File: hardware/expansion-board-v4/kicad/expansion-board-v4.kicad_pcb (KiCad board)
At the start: 6 copper layers, 100 x 62 mm, 174 parts, among them J1 PinHeader_2x20_P2.54mm_Vertic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, J2 U.FL_Hirose_U.FL-R-SMT-1_Vert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, J4 USB_C_Receptacle_HRO_TYPE-C-3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, J5 U.FL_Hirose_U.FL-R-SMT-1_Vert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, J6 U.FL_Hirose_U.FL-R-SMT-1_Vert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, J7 U.FL_Hirose_U.FL-R-SMT-1_Vert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, J8 U.FL_Hirose_U.FL-R-SMT-1_Vert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, J9 MX1.25WT-2P, Q2 SOT-23, Q3 SOT-23, Q4 SOT-23, Q5 SOT-23, SW2 SolderJumper-2_P1.3mm_Open_Pa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, U1 SOT-23-5, U10 QFN-48-1EP_7x7mm_P0.5mm_EP5.1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, U11 DFN-8-1EP_2x2mm_P0.5mm_EP0.86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, U12 SOT-363_SC-70-6, U13 AD8319_LFCSP-8-EP, U14 MSOP-8_3x3mm_P0.65mm, U15 SOT-23-6, U16 SOT-363_SC-70-6, U17 SOT-363_SC-70-6, U18 SOIC-10_3.9x4.9mm_P1mm, U19 QFN-24-1EP_4x4mm_P0.5mm_EP2.6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, U2 SOT-23-5, U20 TSOT-23-6, U3 SOT-23-5, U4 BNO085_LGA-28, U5 BMP388_LGA-10, U6 LGA-16_3x3mm_P0.5mm, U7 ATGM336H_LCC-18, U8 QFN-56-1EP_7x7mm_P0.4mm_EP3.2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, U9 SOIC-8_5.3x5.3mm_P1.27mm, Y1 Crystal_SMD_3225-4Pin_3.2x2.5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, Y2 Crystal_SMD_3225-4Pin_3.2x2.5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, Y3 Crystal_SMD_3215-2Pin_3.2x1.5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

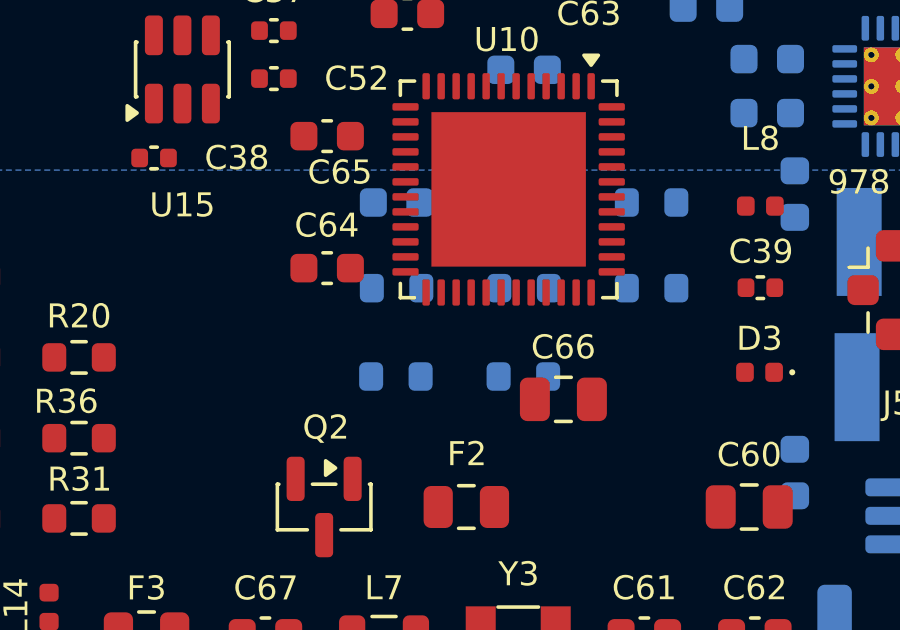
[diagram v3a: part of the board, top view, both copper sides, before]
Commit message: fix(hw): 103AT-2 是插件不是贴片，封装/焊盘/位置全部修正
## 主 bug：RT1 用错封装

103AT-2（SEMITEC 日本石塚）是**轴向引线玻璃封装的插件**，我之前直接套了
R_0603_1608Metric——焊盘、3D、装配全错，根因是没查 datasheet。

改为自建 NTC_103AT-2_Leaded_P2.54mm：两个 ⌀0.7 通孔、间距 2.54mm，
courtyard 只覆盖焊盘不含本体——因为 NTC 玻璃头不留在板面，靠引线延伸
平贴到电池表面。

位置从 (136.93,87.93) 改到 **(125.5,89.5)**，两个判据：
  · CHG_NTC 到分压电阻 R39/R40 只有 4.06mm。这是高阻模拟节点，
    原位置离分压网络 30mm，长走线会耦合开关噪声
  · 焊盘落在电池投影区内，玻璃头平贴板面与电池之间（电池仓净高 11.0
    − 电池 9.5 = 1.5mm 余量，刚好容下 ⌀1.5mm 玻璃头），热耦合最好

选点时扫描了两面 courtyard（通孔件会穿透）、螺丝孔让位圈、天线禁铺区。

## 连带修复：.kicad_mod 不能写 ';;' 注释

上一轮给 MX1.25WT-2P 封装加 3D 说明时用了 ';;'，那是 Lisp 语法，
KiCad 的 S-expression 解析器不认——**整个封装文件直接加载失败**，
而且不报错，只是 FootprintLoad 返回 None。逐个测试库中封装才发现
MX1.25WT-2P 和新建的 NTC 两个都是坏的。注释一律移进 (descr ...)。

## Python 环境：按 CLAUDE.md 用 ServBay

之前 gen_bom_smt.py 报缺 openpyxl，是因为我用了 KiCad 内置的 Python
（那个只该用于需要 pcbnew 的脚本）。ServBay 的 python3 3.13.12 本来就有
openpyxl 3.1.5。现在分工明确：
  · 需要 pcbnew 的（gen_assembly/gen_checklist）→ KiCad Python
  · 纯数据处理的（gen_bom/gen_bom_smt）→ ServBay Python

BOM_采购清单.xlsx（55 项）与 BOM_嘉立创SMT.xlsx（79 料号/162 贴片位）已补出。

## 新增待决项 D3：电源区电容建议 0603 → 0805

不是为了散热（电阻功率算过，R43 最大也才 32.5mW，0603 有 3 倍余量），
而是 DC bias 衰减和耐压可得性：**C72 要 6.8µF/25V，0603 根本买不到**
（0603 在 25V 档容值上限约 1~2.2µF），而它接 9V 侧耐压不能降。
换封装会动 B 面布局，等确认。

验收：原理图↔PCB 封装零不一致，DRC error 0 条，覆铜已重填。
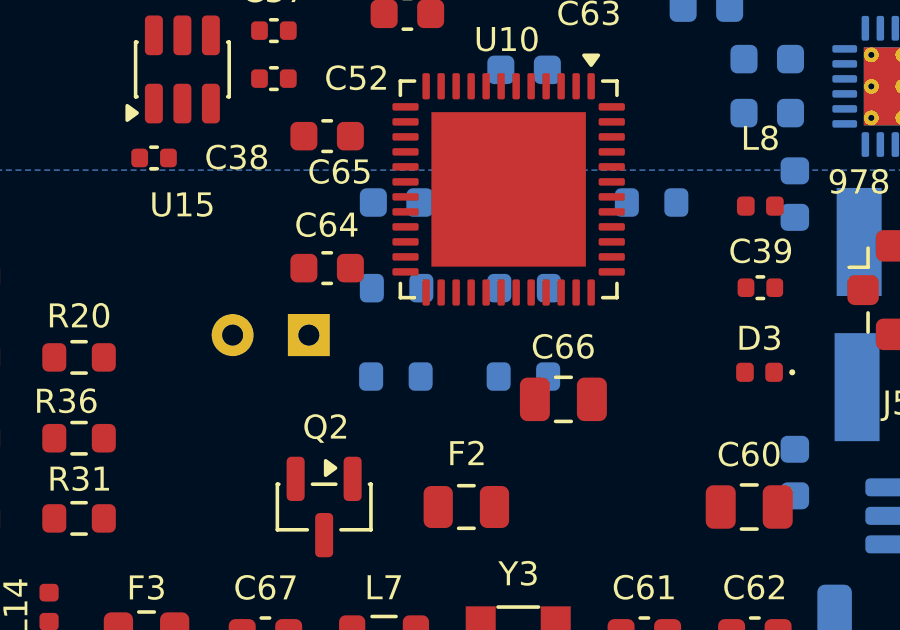
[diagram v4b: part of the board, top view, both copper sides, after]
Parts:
- RT1: value R_0603_1608Metric -> 103AT-2 10k NTC; footprint R_0603_1608Metric -> NTC_103AT-2_Leaded_P2.54mm
- moved RT1 11.5 mm to (125.5, 89.5), turned to 180 degrees
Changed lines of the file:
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@@
 		)
 	)
-	(footprint "R_0603_1608Metric"
+	(footprint "NTC_103AT-2_Leaded_P2.54mm"
 		(layer "B.Cu")
-		(at 136.925 87.9348)
-		(descr "Resistor SMD 0603 (1608 Metric), square (rectangular) end terminal, IPC-7351 nominal, (Body size source: IPC-SM-782 page 72, https://www.pcb-3d.com/wordpress/wp-content/uploads/ipc-sm-782a_amendment_1_and_2.pdf)")
-		(tags "resistor")
+		(at 125.5 89.5 180)
+		(descr "103AT-2 / 103AP-2 热敏电阻（SEMITEC 日本石塚）的板上焊盘。这是**轴向引线玻璃封装的插件**，不是贴片——2026-08-23 之前误用了 R_0603_1608Metric，焊盘和 3D 全错。玻璃头 ⌀约1.5mm、引线 ⌀0.2mm 长约 25~30mm。本封装只画两个通孔焊盘：NTC 本体**不留在板面**，靠引线延伸贴到电池表面并用胶带固定，因此 courtyard 只覆盖焊盘、不含器件本体。")
+		(tags "NTC thermistor 103AT-2 THT leaded battery temperature")
 		(property "Reference" "RT1"
-			(at 0.005 -1.4428 0)
+			(at 1.27 2.2 0)
 			(layer "B.SilkS")
 			(effects
@@
 			)
 		)
-		(property "Value" "R_0603_1608Metric"
-			(at 0 -1.43 180)
+		(property "Value" "103AT-2 10k NTC"
+			(at 1.27 -4.4 0)
 			(layer "B.Fab")
 			(effects
 				(font
-					(size 1 1)
+					(size 0.8 0.8)
 					(thickness 0.15)
 				)
@@
 		)
 		(property "Datasheet" ""
-			(at 0 0 180)
+			(at 0 0 0)
 			(layer "B.Fab")
 			(hide yes)
@@
 		)
 		(property "Description" ""
-			(at 0 0 180)
+			(at 0 0 0)
 			(layer "B.Fab")
 			(hide yes)
@@
 			)
 		)
-		(property "KiLib_Generator" "SMD_2terminal_chip_molded"
-			(at 0 0 180)
-			(layer "B.SilkS")
-			(hide yes)
-			(effects
-				(font
-					(size 1 1)
-					(thickness 0.15)
-				)
-				(justify mirror)
-			)
-		)
-		(attr smd)
+		(attr through_hole)
 		(duplicate_pad_numbers_are_jumpers no)
 		(fp_line
-			(start -0.237258 -0.5225)
-			(end 0.237258 -0.5225)
+			(start 3.64 1.1)
+			(end 3.64 -1.1)
 			(stroke
 				(width 0.12)
@@
 		)
 		(fp_line
-			(start -0.237258 0.5225)
-			(end 0.237258 0.5225)
+			(start -1.1 1.1)
+			(end 3.64 1.1)
 			(stroke
 				(width 0.12)
@@
 			(layer "B.SilkS")
 		)
-		(fp_rect
-			(start -1.48 0.73)
-			(end 1.48 -0.73)
+		(fp_line
+			(start -1.1 1.1)
+			(end -1.1 -1.1)
+			(stroke
+				(width 0.12)
+				(type solid)
+			)
+			(layer "B.SilkS")
+		)
+		(fp_line
+			(start -1.1 -1.1)
+			(end 3.64 -1.1)
+			(stroke
+				(width 0.12)
+				(type solid)
+			)
+			(layer "B.SilkS")
+		)
+		(fp_line
+			(start 3.89 1.35)
+			(end 3.89 -1.35)
 			(stroke
 				(width 0.05)
 				(type solid)
 			)
-			(fill no)
 			(layer "B.CrtYd")
 		)
-		(fp_rect
-			(start -0.8 0.4125)
-			(end 0.8 -0.4125)
+		(fp_line
+			(start 3.89 -1.35)
+			(end -1.35 -1.35)
+			(stroke
+				(width 0.05)
+				(type solid)
+			)
+			(layer "B.CrtYd")
+		)
+		(fp_line
+			(start -1.35 1.35)
+			(end 3.89 1.35)
+			(stroke
+				(width 0.05)
+				(type solid)
+			)
+			(layer "B.CrtYd")
+		)
+		(fp_line
+			(start -1.35 -1.35)
+			(end -1.35 1.35)
+			(stroke
+				(width 0.05)
+				(type solid)
+			)
+			(layer "B.CrtYd")
+		)
+		(fp_line
+			(start 3.64 1.1)
+			(end 3.64 -1.1)
 			(stroke
 				(width 0.1)
 				(type solid)
 			)
-			(fill no)
 			(layer "B.Fab")
 		)
-		(fp_text user "${REFERENCE}"
-			(at 0 0 180)
+		(fp_line
+			(start 3.64 -1.1)
+			(end -1.1 -1.1)
+			(stroke
+				(width 0.1)
+				(type solid)
+			)
 			(layer "B.Fab")
+		)
+		(fp_line
+			(start -1.1 1.1)
+			(end 3.64 1.1)
+			(stroke
+				(width 0.1)
+				(type solid)
+			)
+			(layer "B.Fab")
+		)
+		(fp_line
+			(start -1.1 -1.1)
+			(end -1.1 1.1)
+			(stroke
+				(width 0.1)
+				(type solid)
+			)
+			(layer "B.Fab")
+		)
+		(fp_text user "NTC->BAT"
+			(at 1.27 -2.3 0)
+			(layer "B.SilkS")
 			(effects
 				(font
-					(size 0.4 0.4)
-					(thickness 0.06)
+					(size 0.6 0.6)
+					(thickness 0.1)
 				)
 				(justify mirror)
 			)
 		)
-		(pad "1" smd roundrect
-			(at -0.825 0)
-			(size 0.8 0.95)
-			(layers "B.Cu" "B.Mask" "B.Paste")
-			(roundrect_rratio 0.25)
+		(pad "1" thru_hole rect
+			(at 0 0 180)
+			(size 1.4 1.4)
+			(drill 0.7)
+			(layers "*.Cu" "*.Mask")
+			(remove_unused_layers no)
 			(net "CHG_NTC")
 		)
-		(pad "2" smd roundrect
-			(at 0.825 0)
-			(size 0.8 0.95)
-			(layers "B.Cu" "B.Mask" "B.Paste")
-			(roundrect_rratio 0.25)
+		(pad "2" thru_hole circle
+			(at 2.54 0 180)
+			(size 1.4 1.4)
+			(drill 0.7)
+			(layers "*.Cu" "*.Mask")
+			(remove_unused_layers no)
 			(net "GND")
 		)
 		(embedded_fonts no)
-		(model "${KICAD10_3DMODEL_DIR}/Resistor_SMD.3dshapes/R_0603_1608Metric.step"
-			(offset
-				(xyz 0 0 0)
-			)
-			(scale
-				(xyz 1 1 1)
-			)
-			(rotate
-				(xyz 0 0 0)
-			)
-		)
 	)
 	(footprint "R_0603_1608Metric"

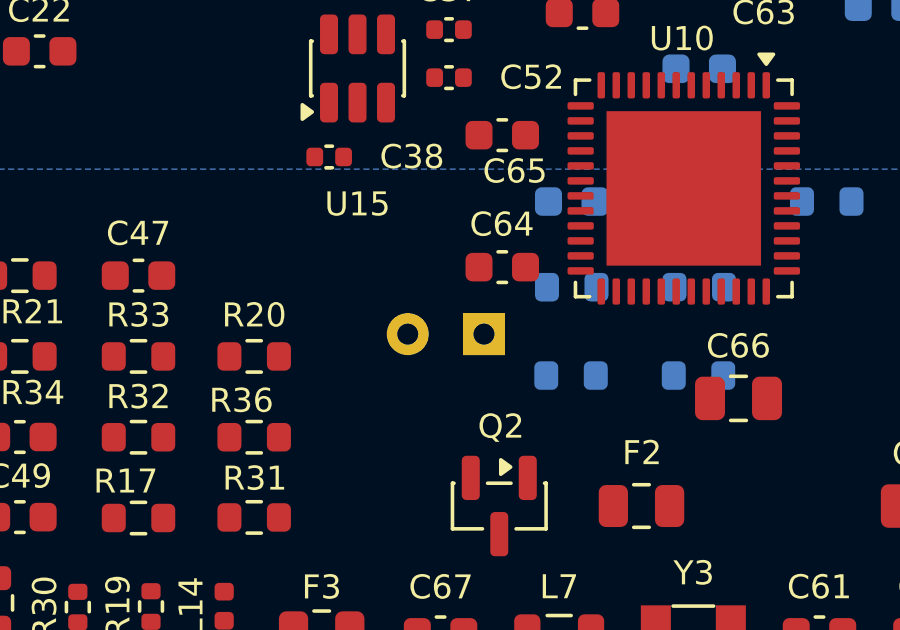
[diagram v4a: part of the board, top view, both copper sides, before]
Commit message: fix(hw): NTC 改用贴片 NCP18XH103F03RB —— 电池是 3M 胶贴死的，插件放不下
## 为什么又改一次

上一轮把 RT1 从 R0603 改成插件封装，理由是「103AT-2 是轴向引线玻璃件」。
那步是对的，但方案错了：**电池用 3M 胶直接贴在 B 面**（防晃动脱落，同时给
背壳散热孔留空间），板面与电池之间**没有间隙**，玻璃头无处安放。
我上一版假设有 1.5mm 余量（11.0 电池仓 − 9.5 电池），那是"电池悬空"的算法，
与实际装配方式不符。

回到贴片，但换成真正的贴片 NTC 型号，不是拿普通电阻封装凑数：
NCP18XH103F03RB（Murata 0603 10k 1%）/ TDK NTCG163JF103FT1 / 国产 0603 10K 1%。

## NTC 本身不能删

SY6970 的 TS 是锂电池充电安全强制项：<0°C 充电析锂（枝晶刺穿隔膜、内短路），
>60°C 加速老化乃至热失控。不接就得用固定电阻假装永远 25°C，等于关掉保护。

座舱 80°C 的担心已查证：TS 保护**只作用于充电路径**。高温时停充，但
PMID→SYS 直供与 BAT→SYS 放电都不受限，设备照常运行，降温自动恢复。
去掉 NTC 才会在 80°C 继续充电，那才是不可预测的后果。

## B 值差异不需要改硬件

103AT-2 是 B25/85=3435K；Murata NCP18XH103 常标 B25/50=3380K，
但同一颗料在 B25/85 口径下是 3428K——差 0.2%，保护阈值偏移 <1°C，
分压电阻 R39/R40 保持不变。要抠精度改 MCU 侧查表/Steinhart-Hart 的 B 参数。

## 位置 (125.25, 88.00)

三个约束一起解出来的：在电池投影区内直接贴电池 / 距板上开关电源 ≥19mm
（否则测的是板温不是电池温）/ CHG_NTC 到分压电阻 R39/R40 仅 4.00mm
（高阻模拟节点，走线长了耦合开关噪声）。

已删除废弃的 NTC_103AT-2_Leaded_P2.54mm 封装，免得下次误用。

验收：DRC error 0 条，原理图↔PCB 一致，全套 BOM/装配文档重生成
（BOM 88 料号、SMT 79 料号 162 贴片位、ASSEMBLY 162 件、CHECKLIST 174 位号）。
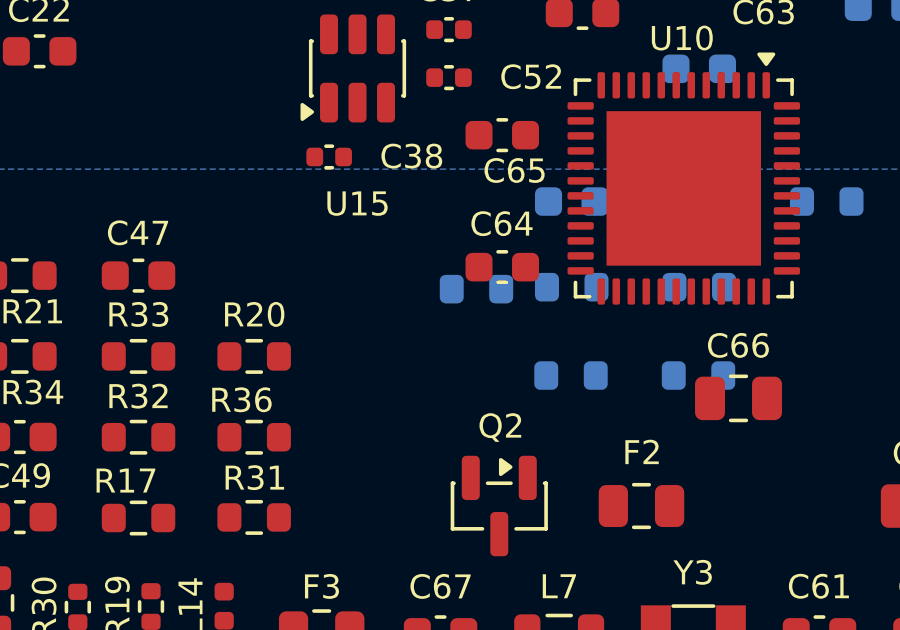
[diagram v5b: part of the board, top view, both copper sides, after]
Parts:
- RT1: value 103AT-2 10k NTC -> NCP18XH103F03RB 10k NTC; footprint NTC_103AT-2_Leaded_P2.54mm -> R_0603_1608Metric
- moved RT1 1.52 mm to (125.2, 88.0)
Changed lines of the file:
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@@
+	(footprint "R_0603_1608Metric"
+		(layer "B.Cu")
+		(at 125.25 88 180)
+		(descr "Resistor SMD 0603 (1608 Metric), square (rectangular) end terminal, IPC-7351 nominal, (Body size source: IPC-SM-782 page 72, https://www.pcb-3d.com/wordpress/wp-content/uploads/ipc-sm-782a_amendment_1_and_2.pdf)")
+		(tags "resistor")
+		(property "Reference" "RT1"
+			(at 0 1.43 0)
+			(layer "B.SilkS")
+			(effects
+				(font
+					(size 1 1)
+					(thickness 0.15)
+				)
+				(justify mirror)
+			)
+		)
+		(property "Value" "NCP18XH103F03RB 10k NTC"
+			(at 0 -1.43 0)
+			(layer "B.Fab")
+			(effects
+				(font
+					(size 1 1)
+					(thickness 0.15)
+				)
+				(justify mirror)
+			)
+		)
+		(property "Datasheet" ""
+			(at 0 0 0)
+			(layer "B.Fab")
+			(hide yes)
+			(effects
+				(font
+					(size 1.27 1.27)
+				)
+				(justify mirror)
+			)
+		)
+		(property "Description" ""
+			(at 0 0 0)
+			(layer "B.Fab")
+			(hide yes)
+			(effects
+				(font
+					(size 1.27 1.27)
+				)
+				(justify mirror)
+			)
+		)
+		(property "KiLib_Generator" "SMD_2terminal_chip_molded"
+			(at 0 0 0)
+			(layer "B.SilkS")
+			(hide yes)
+			(effects
+				(font
+					(size 1 1)
+					(thickness 0.15)
+				)
+				(justify mirror)
+			)
+		)
+		(attr smd)
+		(duplicate_pad_numbers_are_jumpers no)
+		(fp_line
+			(start -0.237258 0.5225)
+			(end 0.237258 0.5225)
+			(stroke
+				(width 0.12)
+				(type solid)
+			)
+			(layer "B.SilkS")
+		)
+		(fp_line
+			(start -0.237258 -0.5225)
+			(end 0.237258 -0.5225)
+			(stroke
+				(width 0.12)
+				(type solid)
+			)
+			(layer "B.SilkS")
+		)
+		(fp_rect
+			(start -1.48 0.73)
+			(end 1.48 -0.73)
+			(stroke
+				(width 0.05)
+				(type solid)
+			)
+			(fill no)
+			(layer "B.CrtYd")
+		)
+		(fp_rect
+			(start -0.8 0.4125)
+			(end 0.8 -0.4125)
+			(stroke
+				(width 0.1)
+				(type solid)
+			)
+			(fill no)
+			(layer "B.Fab")
+		)
+		(fp_text user "${REFERENCE}"
+			(at 0 0 0)
+			(layer "B.Fab")
+			(effects
+				(font
+					(size 0.4 0.4)
+					(thickness 0.06)
+				)
+				(justify mirror)
+			)
+		)
+		(pad "1" smd roundrect
+			(at -0.825 0 180)
+			(size 0.8 0.95)
+			(layers "B.Cu" "B.Mask" "B.Paste")
+			(roundrect_rratio 0.25)
+			(net "CHG_NTC")
+		)
+		(pad "2" smd roundrect
+			(at 0.825 0 180)
+			(size 0.8 0.95)
+			(layers "B.Cu" "B.Mask" "B.Paste")
+			(roundrect_rratio 0.25)
+			(net "GND")
+		)
+		(embedded_fonts no)
+		(model "${KICAD10_3DMODEL_DIR}/Resistor_SMD.3dshapes/R_0603_1608Metric.step"
+			(offset
+				(xyz 0 0 0)
+			)
+			(scale
+				(xyz 1 1 1)
+			)
+			(rotate
+				(xyz 0 0 0)
+			)
+		)
+	)
 	(footprint "R_0603_1608Metric"
 		(layer "B.Cu")
@@
 		)
 	)
-	(footprint "NTC_103AT-2_Leaded_P2.54mm"
-		(layer "B.Cu")
-		(at 125.5 89.5 180)
-		(descr "103AT-2 / 103AP-2 热敏电阻（SEMITEC 日本石塚）的板上焊盘。这是**轴向引线玻璃封装的插件**，不是贴片——2026-08-23 之前误用了 R_0603_1608Metric，焊盘和 3D 全错。玻璃头 ⌀约1.5mm、引线 ⌀0.2mm 长约 25~30mm。本封装只画两个通孔焊盘：NTC 本体**不留在板面**，靠引线延伸贴到电池表面并用胶带固定，因此 courtyard 只覆盖焊盘、不含器件本体。")
-		(tags "NTC thermistor 103AT-2 THT leaded battery temperature")
-		(property "Reference" "RT1"
-			(at 1.27 2.2 0)
-			(layer "B.SilkS")
-			(effects
-				(font
-					(size 0.8 0.8)
-					(thickness 0.15)
-				)
-				(justify mirror)
-			)
-		)
-		(property "Value" "103AT-2 10k NTC"
-			(at 1.27 -4.4 0)
-			(layer "B.Fab")
-			(effects
-				(font
-					(size 0.8 0.8)
-					(thickness 0.15)
-				)
-				(justify mirror)
-			)
-		)
-		(property "Datasheet" ""
-			(at 0 0 0)
-			(layer "B.Fab")
-			(hide yes)
-			(effects
-				(font
-					(size 1.27 1.27)
-				)
-				(justify mirror)
-			)
-		)
-		(property "Description" ""
-			(at 0 0 0)
-			(layer "B.Fab")
-			(hide yes)
-			(effects
-				(font
-					(size 1.27 1.27)
-				)
-				(justify mirror)
-			)
-		)
-		(attr through_hole)
-		(duplicate_pad_numbers_are_jumpers no)
-		(fp_line
-			(start 3.64 1.1)
-			(end 3.64 -1.1)
-			(stroke
-				(width 0.12)
-				(type solid)
-			)
-			(layer "B.SilkS")
-		)
-		(fp_line
-			(start -1.1 1.1)
-			(end 3.64 1.1)
-			(stroke
-				(width 0.12)
-				(type solid)
-			)
-			(layer "B.SilkS")
-		)
-		(fp_line
-			(start -1.1 1.1)
-			(end -1.1 -1.1)
-			(stroke
-				(width 0.12)
-				(type solid)
-			)
-			(layer "B.SilkS")
-		)
-		(fp_line
-			(start -1.1 -1.1)
-			(end 3.64 -1.1)
-			(stroke
-				(width 0.12)
-				(type solid)
-			)
-			(layer "B.SilkS")
-		)
-		(fp_line
-			(start 3.89 1.35)
-			(end 3.89 -1.35)
-			(stroke
-				(width 0.05)
-				(type solid)
-			)
-			(layer "B.CrtYd")
-		)
-		(fp_line
-			(start 3.89 -1.35)
-			(end -1.35 -1.35)
-			(stroke
-				(width 0.05)
-				(type solid)
-			)
-			(layer "B.CrtYd")
-		)
-		(fp_line
-			(start -1.35 1.35)
-			(end 3.89 1.35)
-			(stroke
-				(width 0.05)
-				(type solid)
-			)
-			(layer "B.CrtYd")
-		)
-		(fp_line
-			(start -1.35 -1.35)
-			(end -1.35 1.35)
-			(stroke
-				(width 0.05)
-				(type solid)
-			)
-			(layer "B.CrtYd")
-		)
-		(fp_line
-			(start 3.64 1.1)
-			(end 3.64 -1.1)
-			(stroke
-				(width 0.1)
-				(type solid)
-			)
-			(layer "B.Fab")
-		)
-		(fp_line
-			(start 3.64 -1.1)
-			(end -1.1 -1.1)
-			(stroke
-				(width 0.1)
-				(type solid)
-			)
-			(layer "B.Fab")
-		)
-		(fp_line
-			(start -1.1 1.1)
-			(end 3.64 1.1)
-			(stroke
-				(width 0.1)
-				(type solid)
-			)
-			(layer "B.Fab")
-		)
-		(fp_line
-			(start -1.1 -1.1)
-			(end -1.1 1.1)
-			(stroke
-				(width 0.1)
-				(type solid)
-			)
-			(layer "B.Fab")
-		)
-		(fp_text user "NTC->BAT"
-			(at 1.27 -2.3 0)
-			(layer "B.SilkS")
-			(effects
-				(font
-					(size 0.6 0.6)
-					(thickness 0.1)
-				)
-				(justify mirror)
-			)
-		)
-		(pad "1" thru_hole rect
-			(at 0 0 180)
-			(size 1.4 1.4)
-			(drill 0.7)
-			(layers "*.Cu" "*.Mask")
-			(remove_unused_layers no)
-			(net "CHG_NTC")
-		)
-		(pad "2" thru_hole circle
-			(at 2.54 0 180)
-			(size 1.4 1.4)
-			(drill 0.7)
-			(layers "*.Cu" "*.Mask")
-			(remove_unused_layers no)
-			(net "GND")
-		)
-		(embedded_fonts no)
-	)
 	(footprint "R_0603_1608Metric"
